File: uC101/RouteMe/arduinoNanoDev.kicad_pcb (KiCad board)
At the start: 2 copper layers, 31 parts, among them J1 FTDI (Serial), J2 SPI Header, J3 I2C Header, J4 SAO_Conn, SW1 SW_Push, SW2 Rotary_Encoder_Switch, SW3 SW_Push

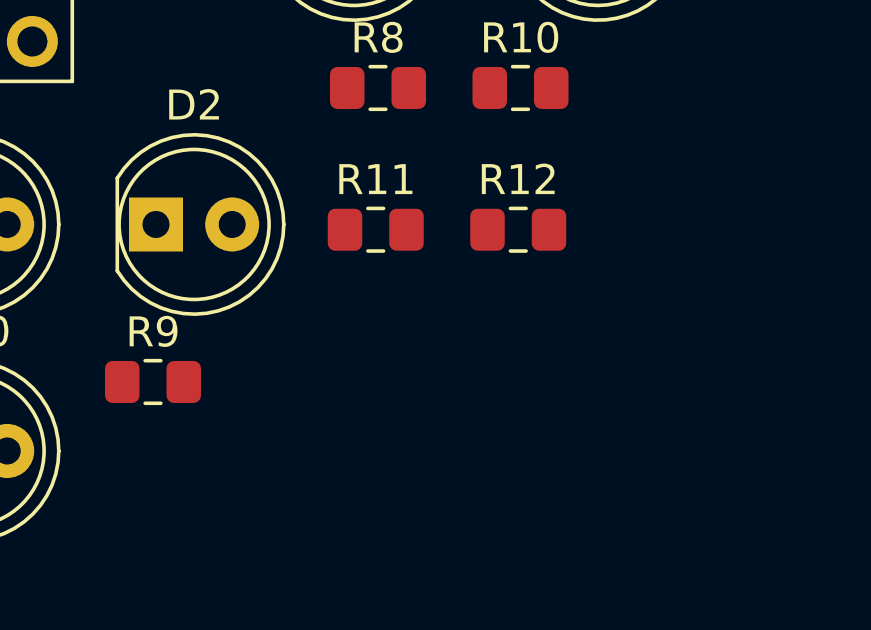
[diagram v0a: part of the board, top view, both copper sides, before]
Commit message: added more slides and resources, small routing changes
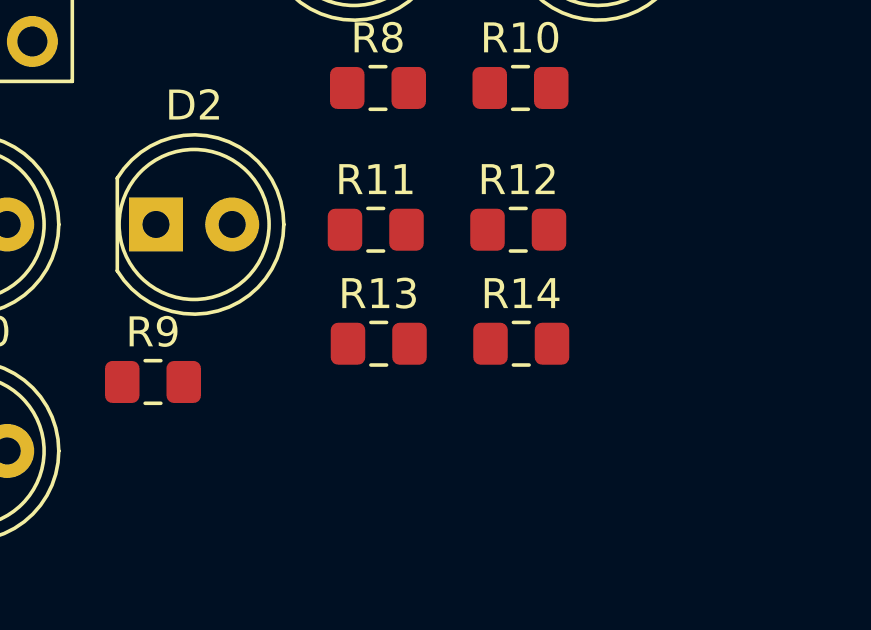
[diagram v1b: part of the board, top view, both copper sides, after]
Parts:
- added R13: 10K, Resistor_SMD:R_0805_2012Metric_Pad1.15x1.40mm_HandSolder, F.Cu at (84.2, 48.4)
- added R14: 10K, Resistor_SMD:R_0805_2012Metric_Pad1.15x1.40mm_HandSolder, F.Cu at (89.0, 48.4)
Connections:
- A1 pad 17: (no net) -> +3V3
- J4 pad 1: +5V -> +3V3
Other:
- rule solder_mask_min_width: 0.25 -> 0.1

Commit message: More board changes + updated RouteMe with latest netlist
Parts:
- added J10: Conn_01x04, uC101:PinHole_1x04_P2.54mm_Vertical, F.Cu at (196.6, 76.5)
- added J11: Conn_01x04, uC101:PinHole_1x04_P2.54mm_Vertical, F.Cu at (192.0, 76.5)
- added J5: Conn_01x10, uC101:PinHole_1x10_P2.54mm_Vertical, F.Cu at (182.7, 49.0)
- added J6: Conn_01x10, uC101:PinHole_1x10_P2.54mm_Vertical, F.Cu at (187.3, 49.0)
- added J7: Conn_01x10, uC101:PinHole_1x10_P2.54mm_Vertical, F.Cu at (196.6, 49.0)
- added J8: Conn_01x10, uC101:PinHole_1x10_P2.54mm_Vertical, F.Cu at (192.0, 49.0)
- added J9: Conn_01x04, uC101:PinHole_1x04_P2.54mm_Vertical, F.Cu at (205.9, 65.5)
- added TP1: ENC_B(D7), TestPoint:TestPoint_Pad_D1.0mm, F.Cu at (200.5, 78.3)
- added TP10: BLUE, TestPoint:TestPoint_Pad_D1.0mm, F.Cu at (234.2, 71.9)
- added TP11: GREEN, TestPoint:TestPoint_Pad_D1.0mm, F.Cu at (240.1, 66.4)
- added TP12: POT, TestPoint:TestPoint_Pad_D1.0mm, F.Cu at (217.3, 89.6)
- added TP13: GND, TestPoint:TestPoint_THTPad_D1.5mm_Drill0.7mm, F.Cu at (200.7, 71.9)
- added TP14: GND, TestPoint:TestPoint_THTPad_D1.5mm_Drill0.7mm, F.Cu at (200.7, 68.4)
- added TP15: ENC_SW(D9), TestPoint:TestPoint_Pad_D1.0mm, F.Cu at (200.5, 75.2)
- added TP2: B1, TestPoint:TestPoint_Pad_D1.0mm, F.Cu at (186.5, 90.5)
- added TP3: ENC_A(D8), TestPoint:TestPoint_Pad_D1.0mm, F.Cu at (203.5, 76.9)
- added TP4: B2, TestPoint:TestPoint_Pad_D1.0mm, F.Cu at (206.6, 76.9)
- added TP5: C1, TestPoint:TestPoint_Pad_D1.0mm, F.Cu at (220.2, 83.7)
- added TP6: C2, TestPoint:TestPoint_Pad_D1.0mm, F.Cu at (231.2, 71.9)
- added TP7: C3, TestPoint:TestPoint_Pad_D1.0mm, F.Cu at (240.1, 63.3)
- added TP8: C4, TestPoint:TestPoint_Pad_D1.0mm, F.Cu at (214.2, 89.9)
- added TP9: RED, TestPoint:TestPoint_Pad_D1.0mm, F.Cu at (231.2, 74.9)
- J1: value FTDI (Serial) -> Serial / UART
- J2: footprint Connector_PinHeader_2.54mm:PinHeader_1x06_P2.54mm_Vertical -> Connector_PinHeader_2.54mm:PinHeader_1x07_P2.54mm_Vertical
- J3: footprint Connector_PinHeader_2.54mm:PinHeader_1x04_P2.54mm_Vertical -> Connector_PinHeader_2.54mm:PinHeader_1x05_P2.54mm_Vertical
- SW2: value Rotary_Encoder_Switch -> SW_Push; footprint Rotary_Encoder:RotaryEncoder_Alps_EC11E-Switch_Vertical_H20mm_CircularMountingHoles -> Button_Switch_THT:SW_PUSH_6mm_H4.3mm
- SW3: value SW_Push -> Rotary_Encoder_Switch; footprint Button_Switch_THT:SW_PUSH_6mm_H4.3mm -> Rotary_Encoder:RotaryEncoder_Alps_EC11E-Switch_Vertical_H20mm_CircularMountingHoles
- moved R2 186.0 mm to (242.6, 51.1)
- moved D9 179.2 mm to (228.8, 66.6)
- moved D3 175.0 mm to (224.6, 59.0)
- moved SW1 175.0 mm to (224.2, 48.7)
- moved D10 170.4 mm to (239.6, 58.0)
- moved R6 168.0 mm to (224.5, 80.7)
- moved SW2 165.1 mm to (210.3, 65.2)
- moved SW3 156.8 mm to (205.6, 52.4)
- moved R8 153.9 mm to (236.2, 64.3)
- moved D7 153.9 mm to (235.2, 50.5)
- moved R4 153.7 mm to (219.7, 80.7)
- moved RV1 153.7 mm to (212.8, 76.3)
- moved D4 153.4 mm to (232.1, 59.0)
- moved R9 152.3 mm to (227.3, 72.2)
- moved R5 149.9 mm to (210.3, 89.8)
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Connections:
- A1 pad 10: /ENCODER_A -> /ENCODER_B
- A1 pad 11: /ENCODER_B -> /ENCODER_A
- A1 pad 13: /SS -> /nSS
- A1 pad 19: /CHARILE_1 -> /CHARILE_3
- A1 pad 20: /CHARILE_2 -> /CHARILE_4
- A1 pad 21: /CHARILE_3 -> /CHARILE_2
- A1 pad 22: /CHARILE_4 -> /CHARILE_1
- J2 pad 1: +5V -> +3V3
- J2 pad 2: /SS -> +5V
- J2 pad 3: /MOSI -> /SCK
- J2 pad 5: /SCK -> /MOSI
- J2 pad 6: GND -> /nSS
- J3 pad 1: +5V -> +3V3
- J3 pad 2: /SDA -> +5V
- J3 pad 3: /SCL -> /SDA
- J3 pad 4: GND -> /SCL
